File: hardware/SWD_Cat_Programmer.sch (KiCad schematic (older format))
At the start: 25 parts, among them J1 DEBUG_OUT, P1 USB_C_Plug_USB2.0, SW1 RST, SW2 BOOT, U1 CH552G, U2 HX9193-33GB

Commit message: pin output changed
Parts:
- removed J1: DEBUG_OUT, Connector_PinHeader_2.54mm:PinHeader_2x05_P2.54mm_Horizontal, symbol Connector_Generic:Conn_02x05_Odd_Even
- added J1: DEBUG_OUTPUT, Connector_PinHeader_2.54mm:PinHeader_1x05_P2.54mm_Horizontal, symbol Connector_Generic:Conn_01x05
- U1: symbol SWD_Cat_Programmer-rescue:CH552G-Electronic_Cats -> SWD_Cat_Programmer-rescue:CH552G-Electronic_Cats-SWD_Cat_Programmer-rescue
- U2: value HX9193-33GB -> AP2112K-3.3
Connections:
- wire segments 88 -> 82
- no-connect marks 10 -> 6
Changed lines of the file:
@@
 Title "CMIS DAP Cat Programmer"
 Date "2020-08-07"
-Rev "1.0"
+Rev "1.1"
 Comp "Electronic Cats"
 Comment1 ""
@@
 F 3 "https://www.usb.org/sites/default/files/documents/usb_type-c.zip" H 1830 2310 50  0001 C CNN
 	1    1680 2310
-	1    0    0    -1
-$EndComp
-$Comp
-L Connector_Generic:Conn_02x05_Odd_Even J1
-U 1 1 5F2680CE
-P 9605 1880
-F 0 "J1" H 9655 2297 50  0000 C CNN
-F 1 "DEBUG_OUT" H 9655 2206 50  0000 C CNN
-F 2 "Connector_PinHeader_2.54mm:PinHeader_2x05_P2.54mm_Horizontal" H 9605 1880 50  0001 C CNN
-F 3 "~" H 9605 1880 50  0001 C CNN
-	1    9605 1880
 	1    0    0    -1
 $EndComp
@@
 $EndComp
 $Comp
-L SWD_Cat_Programmer-rescue:CH552G-Electronic_Cats U1
+L SWD_Cat_Programmer-rescue:CH552G-Electronic_Cats-SWD_Cat_Programmer-rescue U1
 U 1 1 5F26B9A6
 P 5030 2390
@@
 Text Label 8110 3865 0    50   ~ 0
 RST
-Text Label 9905 1680 0    50   ~ 0
+Text Label 9405 1780 2    50   ~ 0
 SWDIO
-Text Label 9905 1780 0    50   ~ 0
+Text Label 9405 1880 2    50   ~ 0
 SWCLK
-Text Label 9905 2080 0    50   ~ 0
+Text Label 9405 2080 2    50   ~ 0
 RESET
-Wire Wire Line
-	9405 1780 9195 1780
-Wire Wire Line
-	9195 1780 9195 1880
-Wire Wire Line
-	9405 1880 9195 1880
-Connection ~ 9195 1880
-Wire Wire Line
-	9195 1880 9195 2065
 $Comp
 L power:GND #PWR013
 U 1 1 5F27EA9C
-P 9195 2325
-F 0 "#PWR013" H 9195 2075 50  0001 C CNN
-F 1 "GND" H 9200 2152 50  0000 C CNN
-F 2 "" H 9195 2325 50  0001 C CNN
-F 3 "" H 9195 2325 50  0001 C CNN
-	1    9195 2325
+P 9100 2125
+F 0 "#PWR013" H 9100 1875 50  0001 C CNN
+F 1 "GND" H 9105 1952 50  0000 C CNN
+F 2 "" H 9100 2125 50  0001 C CNN
+F 3 "" H 9100 2125 50  0001 C CNN
+	1    9100 2125
 	1    0    0    -1
 $EndComp
@@
 NoConn ~ 5380 2940
 $Comp
-L Regulator_Linear:AP2112K-3.3 U2
-U 1 1 5F292947
-P 9695 5595
-F 0 "U2" H 9695 5937 50  0000 C CNN
-F 1 "HX9193-33GB" H 9695 5846 50  0000 C CNN
-F 2 "Package_TO_SOT_SMD:SOT-23-5" H 9695 5920 50  0001 C CNN
-F 3 "https://lcsc.com/product-detail/Low-Dropout-Regulators-LDO_HX-hengjiaxing-HX9193-33GB_C296123.html" H 9695 5695 50  0001 C CNN
-	1    9695 5595
-	1    0    0    -1
-$EndComp
-$Comp
 L power:+3V3 #PWR012
 U 1 1 5F2A3F1C
-P 9105 1580
-F 0 "#PWR012" H 9105 1430 50  0001 C CNN
-F 1 "+3V3" H 9120 1753 50  0000 C CNN
-F 2 "" H 9105 1580 50  0001 C CNN
-F 3 "" H 9105 1580 50  0001 C CNN
-	1    9105 1580
-	1    0    0    -1
-$EndComp
-Wire Wire Line
-	9405 1680 9105 1680
-Wire Wire Line
-	9105 1680 9105 1580
-Wire Wire Line
-	8760 1690 9105 1690
-Wire Wire Line
-	9105 1690 9105 1680
+P 9175 1640
+F 0 "#PWR012" H 9175 1490 50  0001 C CNN
+F 1 "+3V3" H 9190 1813 50  0000 C CNN
+F 2 "" H 9175 1640 50  0001 C CNN
+F 3 "" H 9175 1640 50  0001 C CNN
+	1    9175 1640
+	1    0    0    -1
+$EndComp
 Wire Wire Line
 	8760 1690 8760 1755
-Connection ~ 9105 1680
 Wire Wire Line
 	8760 1955 8760 2065
-Wire Wire Line
-	8760 2065 9195 2065
-Connection ~ 9195 2065
-Wire Wire Line
-	9195 2065 9195 2325
-NoConn ~ 9405 1980
-NoConn ~ 9905 1980
-NoConn ~ 9905 1880
-NoConn ~ 9405 2080
 Wire Notes Line
 	3255 7770 3255 475
@@
 Wire Wire Line
 	3835 2440 3835 2315
+$Comp
+L Regulator_Linear:AP2112K-3.3 U2
+U 1 1 5F4DC1B0
+P 9695 5595
+F 0 "U2" H 9695 5937 50  0000 C CNN
+F 1 "AP2112K-3.3" H 9695 5846 50  0000 C CNN
+F 2 "Package_TO_SOT_SMD:SOT-23-5" H 9695 5920 50  0001 C CNN
+F 3 "https://www.diodes.com/assets/Datasheets/AP2112.pdf" H 9695 5695 50  0001 C CNN
+	1    9695 5595
+	1    0    0    -1
+$EndComp
+$Comp
+L Connector_Generic:Conn_01x05 J1
+U 1 1 5F4EF801
+P 9605 1880
+F 0 "J1" H 9685 1922 50  0000 L CNN
+F 1 "DEBUG_OUTPUT" H 9325 2230 50  0000 L CNN
+F 2 "Connector_PinHeader_2.54mm:PinHeader_1x05_P2.54mm_Horizontal" H 9605 1880 50  0001 C CNN
+F 3 "~" H 9605 1880 50  0001 C CNN
+	1    9605 1880
+	1    0    0    -1
+$EndComp
+Wire Wire Line
+	9405 1680 9175 1680
+Wire Wire Line
+	9175 1680 9175 1640
+Wire Wire Line
+	9100 2125 9100 1980
+Wire Wire Line
+	9100 1980 9405 1980
+$Comp
+L power:+3V3 #PWR019
+U 1 1 5F4F7B85
+P 8760 1690
+F 0 "#PWR019" H 8760 1540 50  0001 C CNN
+F 1 "+3V3" H 8775 1863 50  0000 C CNN
+F 2 "" H 8760 1690 50  0001 C CNN
+F 3 "" H 8760 1690 50  0001 C CNN
+	1    8760 1690
+	1    0    0    -1
+$EndComp
+$Comp
+L power:GND #PWR020
+U 1 1 5F4F8184
+P 8760 2065
+F 0 "#PWR020" H 8760 1815 50  0001 C CNN
+F 1 "GND" H 8765 1892 50  0000 C CNN
+F 2 "" H 8760 2065 50  0001 C CNN
+F 3 "" H 8760 2065 50  0001 C CNN
+	1    8760 2065
+	1    0    0    -1
+$EndComp
 $EndSCHEMATC

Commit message: v1.1 align
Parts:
- U1: symbol SWD_Cat_Programmer-rescue:CH552G-Electronic_Cats-SWD_Cat_Programmer-rescue -> SWD_Cat_Programmer-rescue:CH552G-Electronic_Cats-SWD_Cat_Programmer-rescue-SWD_Cat_Programmer-rescue
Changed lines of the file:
@@
 Sheet 1 1
 Title "CMIS DAP Cat Programmer"
-Date "2020-08-07"
+Date "2020-09-01"
 Rev "1.1"
 Comp "Electronic Cats"
 Comment1 ""
-Comment2 "Eduaro Wero"
+Comment2 "Eduaro Contreras"
 Comment3 "Felipe Islas"
 Comment4 "Andres Sabas"
@@
 $EndComp
 $Comp
-L SWD_Cat_Programmer-rescue:CH552G-Electronic_Cats-SWD_Cat_Programmer-rescue U1
+L SWD_Cat_Programmer-rescue:CH552G-Electronic_Cats-SWD_Cat_Programmer-rescue-SWD_Cat_Programmer-rescue U1
 U 1 1 5F26B9A6
 P 5030 2390

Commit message: update some data
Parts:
- C1, C2, C3: manf# (none) -> C49678
- C4, C5: manf# (none) -> C28323
- D1, D2: manf# (none) -> C131244
- J1: manf# (none) -> -
- P1: manf# (none) -> C393939
- R1, R2: manf# (none) -> C105874
- R10, R11, R9: manf# (none) -> C429431
- R3, R4, R5: manf# (none) -> C103997
- R6: manf# (none) -> C702832
- R7, R8: manf# (none) -> C25623
- SW1, SW2: manf# (none) -> C455281
- U1: symbol SWD_Cat_Programmer-rescue:CH552G-Electronic_Cats-SWD_Cat_Programmer-rescue-SWD_Cat_Programmer-rescue -> SWD_Cat_Programmer-rescue:CH552G-Electronic_Cats-SWD_Cat_Programmer-rescue-SWD_Cat_Programmer-rescue-SWD_Cat_Programmer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; manf# (none) -> C111292
- U2: manf# (none) -> 621-AP2112K-3.3TRG1
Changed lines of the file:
@@
 F 1 "USB_C_Plug_USB2.0" H 1787 3086 50  0000 C CNN
 F 2 "Connectors:C393939" H 1830 2310 50  0001 C CNN
-F 3 "https://www.usb.org/sites/default/files/documents/usb_type-c.zip" H 1830 2310 50  0001 C CNN
+F 3 "https://datasheet.lcsc.com/szlcsc/1912111437_SHOU-HAN-TYPE-C16PIN_C393939.pdf" H 1830 2310 50  0001 C CNN
+F 4 "C393939" H 1680 2310 50  0001 C CNN "manf#"
 	1    1680 2310
 	1    0    0    -1
@@
 F 1 "0.1uF" H 8852 1810 50  0000 L CNN
 F 2 "Capacitor_SMD:C_0805_2012Metric_Pad1.15x1.40mm_HandSolder" H 8760 1855 50  0001 C CNN
-F 3 "~" H 8760 1855 50  0001 C CNN
+F 3 "https://datasheet.lcsc.com/szlcsc/1810101813_YAGEO-CC0805KRX7R9BB104_C49678.pdf" H 8760 1855 50  0001 C CNN
+F 4 "C49678" H 8760 1855 50  0001 C CNN "manf#"
 	1    8760 1855
 	1    0    0    -1
@@
 F 1 "5.1K" V 2405 2000 50  0000 C CNN
 F 2 "Resistor_SMD:R_0805_2012Metric_Pad1.15x1.40mm_HandSolder" H 2470 1910 50  0001 C CNN
-F 3 "~" H 2470 1910 50  0001 C CNN
+F 3 "https://datasheet.lcsc.com/szlcsc/1810311431_YAGEO-RC0805JR-075K1L_C105874.pdf" H 2470 1910 50  0001 C CNN
+F 4 "C105874" V 2470 1910 50  0001 C CNN "manf#"
 	1    2470 1910
 	0    1    1    0
 $EndComp
 $Comp
-L SWD_Cat_Programmer-rescue:CH552G-Electronic_Cats-SWD_Cat_Programmer-rescue-SWD_Cat_Programmer-rescue U1
+L SWD_Cat_Programmer-rescue:CH552G-Electronic_Cats-SWD_Cat_Programmer-rescue-SWD_Cat_Programmer-rescue-SWD_Cat_Programmer-rescue U1
 U 1 1 5F26B9A6
 P 5030 2390
@@
 F 1 "CH552G" H 5055 2724 50  0000 C CNN
 F 2 "Package_SO:SOP-16_4.55x10.3mm_P1.27mm" H 5030 2390 50  0001 C CNN
-F 3 "" H 5030 2390 50  0001 C CNN
+F 3 "https://datasheet.lcsc.com/szlcsc/2008191734_WCH-Jiangsu-Qin-Heng-CH552G_C111292.pdf" H 5030 2390 50  0001 C CNN
+F 4 "C111292" H 5030 2390 50  0001 C CNN "manf#"
 	1    5030 2390
 	1    0    0    -1
@@
 F 1 "0.1uF" H 4115 2715 50  0000 L CNN
 F 2 "Capacitor_SMD:C_0805_2012Metric_Pad1.15x1.40mm_HandSolder" H 4365 2790 50  0001 C CNN
-F 3 "~" H 4365 2790 50  0001 C CNN
+F 3 "https://datasheet.lcsc.com/szlcsc/1810101813_YAGEO-CC0805KRX7R9BB104_C49678.pdf" H 4365 2790 50  0001 C CNN
+F 4 "C49678" H 4365 2790 50  0001 C CNN "manf#"
 	1    4365 2790
 	1    0    0    -1
@@
 F 1 "0.1uF" H 4355 2480 50  0000 L CNN
 F 2 "Capacitor_SMD:C_0805_2012Metric_Pad1.15x1.40mm_HandSolder" H 4580 2540 50  0001 C CNN
-F 3 "~" H 4580 2540 50  0001 C CNN
+F 3 "https://datasheet.lcsc.com/szlcsc/1810101813_YAGEO-CC0805KRX7R9BB104_C49678.pdf" H 4580 2540 50  0001 C CNN
+F 4 "C49678" H 4580 2540 50  0001 C CNN "manf#"
 	1    4580 2540
 	1    0    0    -1
@@
 F 1 "5.1K" V 2535 2100 50  0000 C CNN
 F 2 "Resistor_SMD:R_0805_2012Metric_Pad1.15x1.40mm_HandSolder" H 2470 2010 50  0001 C CNN
-F 3 "~" H 2470 2010 50  0001 C CNN
+F 3 "https://datasheet.lcsc.com/szlcsc/1810311431_YAGEO-RC0805JR-075K1L_C105874.pdf" H 2470 2010 50  0001 C CNN
+F 4 "C105874" V 2470 2010 50  0001 C CNN "manf#"
 	1    2470 2010
 	0    1    1    0
@@
 F 1 "1K" V 9550 4055 50  0000 C CNN
 F 2 "Resistor_SMD:R_0805_2012Metric_Pad1.15x1.40mm_HandSolder" H 9625 4060 50  0001 C CNN
-F 3 "~" H 9625 4060 50  0001 C CNN
+F 3 "https://datasheet.lcsc.com/szlcsc/1809140835_UNI-ROYAL-Uniroyal-Elec-0805W8J0102T5E_C25623.pdf" H 9625 4060 50  0001 C CNN
+F 4 "C25623" V 9625 4060 50  0001 C CNN "manf#"
 	1    9625 4060
 	0    1    1    0
@@
 F 1 "LED" H 9910 4165 50  0000 C CNN
 F 2 "LED_SMD:LED_0805_2012Metric" H 9920 4060 50  0001 C CNN
-F 3 "~" H 9920 4060 50  0001 C CNN
+F 3 "https://datasheet.lcsc.com/szlcsc/1808272351_Everlight-Elec-17-21SURC-S530-A2-TR8_C131244.pdf" H 9920 4060 50  0001 C CNN
+F 4 "C131244" H 9920 4060 50  0001 C CNN "manf#"
 	1    9920 4060
 	-1   0    0    1
@@
 F 1 "RST" H 7815 4059 50  0000 C CNN
 F 2 "KiCad:TS1088R02026" H 7815 4065 50  0001 C CNN
-F 3 "~" H 7815 4065 50  0001 C CNN
+F 3 "https://datasheet.lcsc.com/szlcsc/1912111437_XUNPU-TS-1088R-02526_C455281.pdf" H 7815 4065 50  0001 C CNN
+F 4 "C455281" H 7815 3865 50  0001 C CNN "manf#"
 	1    7815 3865
 	1    0    0    -1
@@
 F 1 "BOOT" H 7835 4459 50  0000 C CNN
 F 2 "KiCad:TS1088R02026" H 7835 4465 50  0001 C CNN
-F 3 "~" H 7835 4465 50  0001 C CNN
+F 3 "https://datasheet.lcsc.com/szlcsc/1912111437_XUNPU-TS-1088R-02526_C455281.pdf" H 7835 4465 50  0001 C CNN
+F 4 "C455281" H 7835 4265 50  0001 C CNN "manf#"
 	1    7835 4265
 	1    0    0    -1
@@
 F 1 "20K" V 8120 4265 50  0000 C CNN
 F 2 "Resistor_SMD:R_0805_2012Metric_Pad1.15x1.40mm_HandSolder" H 8225 4265 50  0001 C CNN
-F 3 "~" H 8225 4265 50  0001 C CNN
+F 3 "https://datasheet.lcsc.com/szlcsc/2007131613_HKR-Hong-Kong-Resistors-RCT0520KFLF_C702832.pdf" H 8225 4265 50  0001 C CNN
+F 4 "C702832" V 8225 4265 50  0001 C CNN "manf#"
 	1    8225 4265
 	0    1    1    0
@@
 F 1 "150" V 5635 3145 50  0000 C CNN
 F 2 "Resistor_SMD:R_0805_2012Metric_Pad1.15x1.40mm_HandSolder" H 5635 3140 50  0001 C CNN
-F 3 "~" H 5635 3140 50  0001 C CNN
+F 3 "https://datasheet.lcsc.com/szlcsc/1811081415_RALEC-RTT051500FTP_C103997.pdf" H 5635 3140 50  0001 C CNN
+F 4 "C103997" V 5635 3140 50  0001 C CNN "manf#"
 	1    5635 3140
 	0    1    1    0
@@
 F 1 "150" V 5635 3240 50  0000 C CNN
 F 2 "Resistor_SMD:R_0805_2012Metric_Pad1.15x1.40mm_HandSolder" H 5630 3240 50  0001 C CNN
-F 3 "~" H 5630 3240 50  0001 C CNN
+F 3 "https://datasheet.lcsc.com/szlcsc/1811081415_RALEC-RTT051500FTP_C103997.pdf" H 5630 3240 50  0001 C CNN
+F 4 "C103997" V 5630 3240 50  0001 C CNN "manf#"
 	1    5630 3240
 	0    1    1    0
@@
 F 1 "150" V 5700 3340 50  0000 C CNN
 F 2 "Resistor_SMD:R_0805_2012Metric_Pad1.15x1.40mm_HandSolder" H 5630 3340 50  0001 C CNN
-F 3 "~" H 5630 3340 50  0001 C CNN
+F 3 "https://datasheet.lcsc.com/szlcsc/1811081415_RALEC-RTT051500FTP_C103997.pdf" H 5630 3340 50  0001 C CNN
+F 4 "C103997" V 5630 3340 50  0001 C CNN "manf#"
 	1    5630 3340
 	0    1    1    0
@@
 F 1 "1uF" H 9137 5600 50  0000 L CNN
 F 2 "Capacitor_SMD:C_0805_2012Metric_Pad1.15x1.40mm_HandSolder" H 9045 5645 50  0001 C CNN
-F 3 "~" H 9045 5645 50  0001 C CNN
+F 3 "https://datasheet.lcsc.com/szlcsc/1810191216_Samsung-Electro-Mechanics-CL21B105KBFNNNE_C28323.pdf" H 9045 5645 50  0001 C CNN
+F 4 "C28323" H 9045 5645 50  0001 C CNN "manf#"
 	1    9045 5645
 	1    0    0    -1
@@
 F 1 "1uF" H 10187 5550 50  0000 L CNN
 F 2 "Capacitor_SMD:C_0805_2012Metric_Pad1.15x1.40mm_HandSolder" H 10095 5595 50  0001 C CNN
-F 3 "~" H 10095 5595 50  0001 C CNN
+F 3 "https://datasheet.lcsc.com/szlcsc/1810191216_Samsung-Electro-Mechanics-CL21B105KBFNNNE_C28323.pdf" H 10095 5595 50  0001 C CNN
+F 4 "C28323" H 10095 5595 50  0001 C CNN "manf#"
 	1    10095 5595
 	1    0    0    -1
@@
 F 1 "1K" V 9560 3565 50  0000 C CNN
 F 2 "Resistor_SMD:R_0805_2012Metric_Pad1.15x1.40mm_HandSolder" H 9635 3570 50  0001 C CNN
-F 3 "~" H 9635 3570 50  0001 C CNN
+F 3 "https://datasheet.lcsc.com/szlcsc/1809140835_UNI-ROYAL-Uniroyal-Elec-0805W8J0102T5E_C25623.pdf" H 9635 3570 50  0001 C CNN
+F 4 "C25623" V 9635 3570 50  0001 C CNN "manf#"
 	1    9635 3570
 	0    1    1    0
@@
 F 1 "LED" H 9920 3675 50  0000 C CNN
 F 2 "LED_SMD:LED_0805_2012Metric" H 9930 3570 50  0001 C CNN
-F 3 "~" H 9930 3570 50  0001 C CNN
+F 3 "https://datasheet.lcsc.com/szlcsc/1808272351_Everlight-Elec-17-21SURC-S530-A2-TR8_C131244.pdf" H 9930 3570 50  0001 C CNN
+F 4 "C131244" H 9930 3570 50  0001 C CNN "manf#"
 	1    9930 3570
 	-1   0    0    1
@@
 F 2 "Resistor_SMD:R_0603_1608Metric_Pad1.05x0.95mm_HandSolder" H 5890 3000 50  0001 C CNN
 F 3 "~" H 5890 3000 50  0001 C CNN
+F 4 "C429431" V 5890 3000 50  0001 C CNN "manf#"
 	1    5890 3000
 	-1   0    0    1
@@
 F 2 "Resistor_SMD:R_0603_1608Metric_Pad1.05x0.95mm_HandSolder" H 6035 3000 50  0001 C CNN
 F 3 "~" H 6035 3000 50  0001 C CNN
+F 4 "C429431" V 6035 3000 50  0001 C CNN "manf#"
 	1    6035 3000
 	-1   0    0    1
@@
 F 2 "Resistor_SMD:R_0603_1608Metric_Pad1.05x0.95mm_HandSolder" H 6180 3000 50  0001 C CNN
 F 3 "~" H 6180 3000 50  0001 C CNN
+F 4 "C429431" V 6180 3000 50  0001 C CNN "manf#"
 	1    6180 3000
 	-1   0    0    1
@@
 F 1 "AP2112K-3.3" H 9695 5846 50  0000 C CNN
 F 2 "Package_TO_SOT_SMD:SOT-23-5" H 9695 5920 50  0001 C CNN
-F 3 "https://www.diodes.com/assets/Datasheets/AP2112.pdf" H 9695 5695 50  0001 C CNN
+F 3 "https://www.mouser.mx/datasheet/2/115/AP2112-271550.pdf" H 9695 5695 50  0001 C CNN
+F 4 "621-AP2112K-3.3TRG1" H 9695 5595 50  0001 C CNN "manf#"
 	1    9695 5595
 	1    0    0    -1
@@
 F 2 "Connector_PinHeader_2.54mm:PinHeader_1x05_P2.54mm_Horizontal" H 9605 1880 50  0001 C CNN
 F 3 "~" H 9605 1880 50  0001 C CNN
+F 4 "-" H 9605 1880 50  0001 C CNN "manf#"
 	1    9605 1880
 	1    0    0    -1

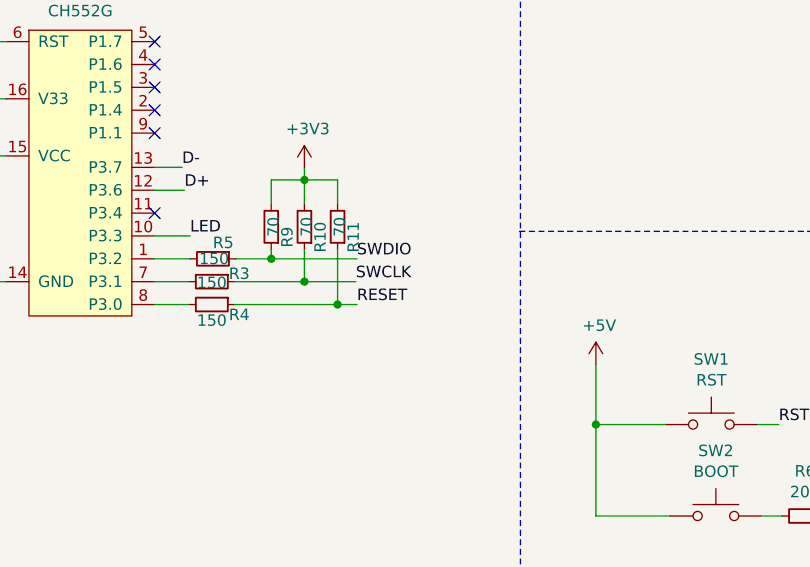
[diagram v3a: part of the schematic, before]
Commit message: Update labels for Serial Adapter
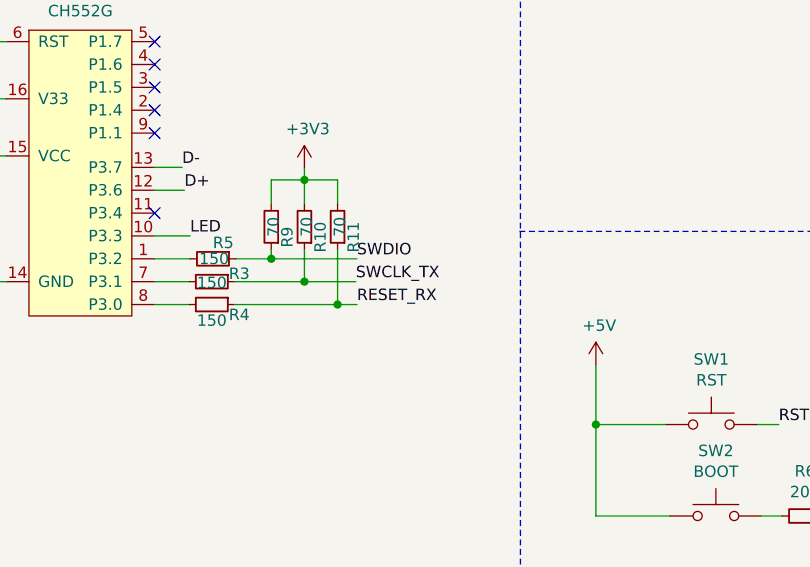
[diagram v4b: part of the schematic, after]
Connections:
- net RESET: no longer R11.1, R4.1
- net SWCLK: no longer R10.1, R3.1
- new net RESET_RX: R11.1, R4.1
- new net SWCLK_TX: R10.1, R3.1
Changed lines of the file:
@@
 SWDIO
 Text Label 6260 3240 0    50   ~ 0
-SWCLK
-Text Label 6265 3340 0    50   ~ 0
-RESET
+SWCLK_TX
 $Comp
 L Device:R_Small R5
@@
 	1    0    0    -1
 $EndComp
+Text Label 6265 3340 0    50   ~ 0
+RESET_RX
 $EndSCHEMATC
